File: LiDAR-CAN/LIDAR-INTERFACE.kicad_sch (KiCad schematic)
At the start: 31 parts, among them U3 W5500, Y1 25MHz

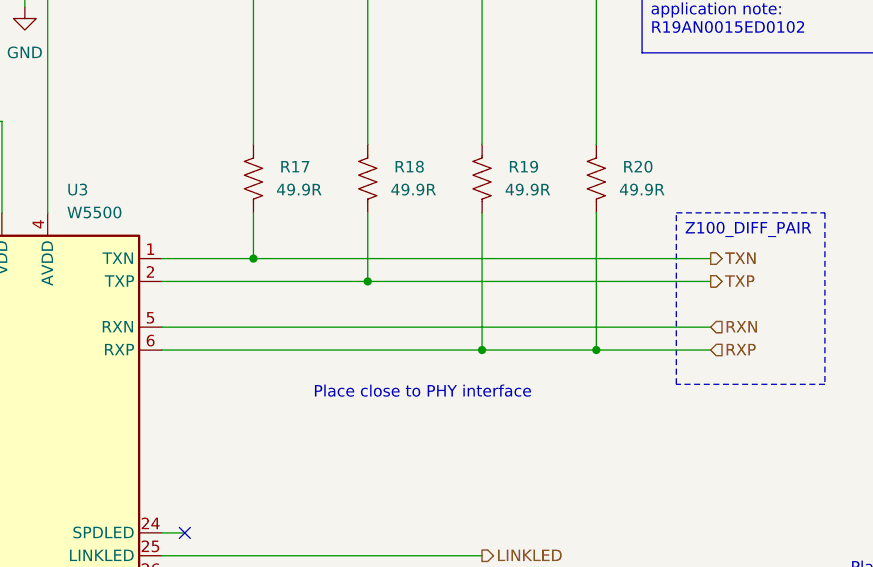
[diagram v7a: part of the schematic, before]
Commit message: Add CAN and MCU placement
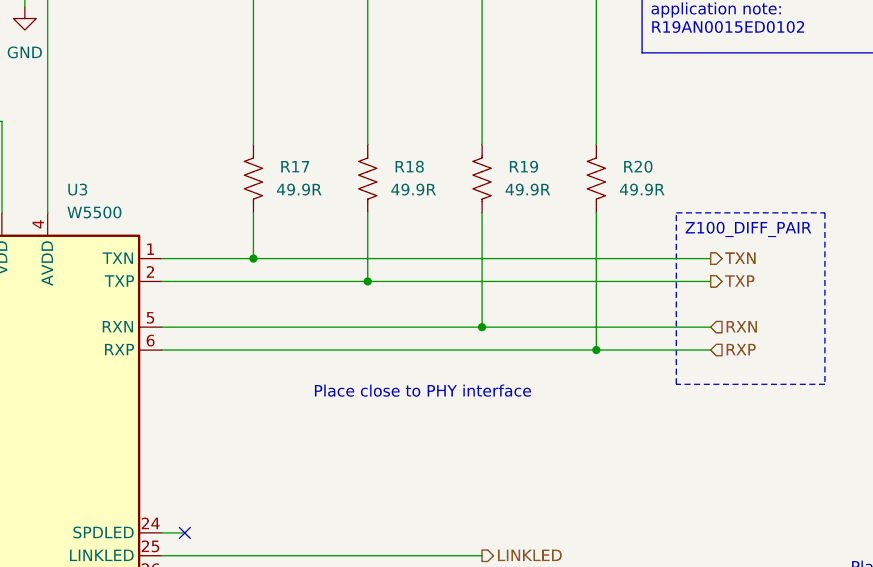
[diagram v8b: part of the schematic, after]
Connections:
- net RXN: now also R19.1
- net RXP: no longer R19.1
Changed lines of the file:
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@@
-	)
-	(junction
-		(at 190.5 101.6)
-		(diameter 0)
-		(color 0 0 0 0)
 	)
 	(junction
@@
 	(junction
 		(at 142.24 50.8)
+		(diameter 0)
+		(color 0 0 0 0)
+	)
+	(junction
+		(at 190.5 99.06)
 		(diameter 0)
 		(color 0 0 0 0)
@@
 	(wire
 		(pts
+			(xy 190.5 99.06) (xy 215.9 99.06)
+		)
+		(stroke
+			(width 0)
+			(type default)
+		)
+	)
+	(wire
+		(pts
 			(xy 158.75 151.13) (xy 158.75 152.4)
 		)
@@
 	(wire
 		(pts
+			(xy 190.5 86.36) (xy 190.5 99.06)
+		)
+		(stroke
+			(width 0)
+			(type default)
+		)
+	)
+	(wire
+		(pts
 			(xy 80.01 139.7) (xy 88.9 139.7)
 		)
@@
 	(wire
 		(pts
-			(xy 190.5 101.6) (xy 203.2 101.6)
-		)
-		(stroke
-			(width 0)
-			(type default)
-		)
-	)
-	(wire
-		(pts
 			(xy 72.39 139.7) (xy 69.85 139.7)
 		)
@@
 	(wire
 		(pts
-			(xy 190.5 86.36) (xy 190.5 101.6)
-		)
-		(stroke
-			(width 0)
-			(type default)
-		)
-	)
-	(wire
-		(pts
 			(xy 88.9 50.8) (xy 101.6 50.8)
 		)
@@
 	(wire
 		(pts
-			(xy 154.94 99.06) (xy 215.9 99.06)
+			(xy 154.94 99.06) (xy 190.5 99.06)
 		)
 		(stroke
@@
 	(wire
 		(pts
-			(xy 154.94 101.6) (xy 190.5 101.6)
-		)
-		(stroke
+			(xy 154.94 101.6) (xy 203.2 101.6)
+		)
+		(stroke
